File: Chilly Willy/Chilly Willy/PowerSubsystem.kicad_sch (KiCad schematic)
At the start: 8 parts, among them J1 Conn_01x03, U1 BK_HTC-15M

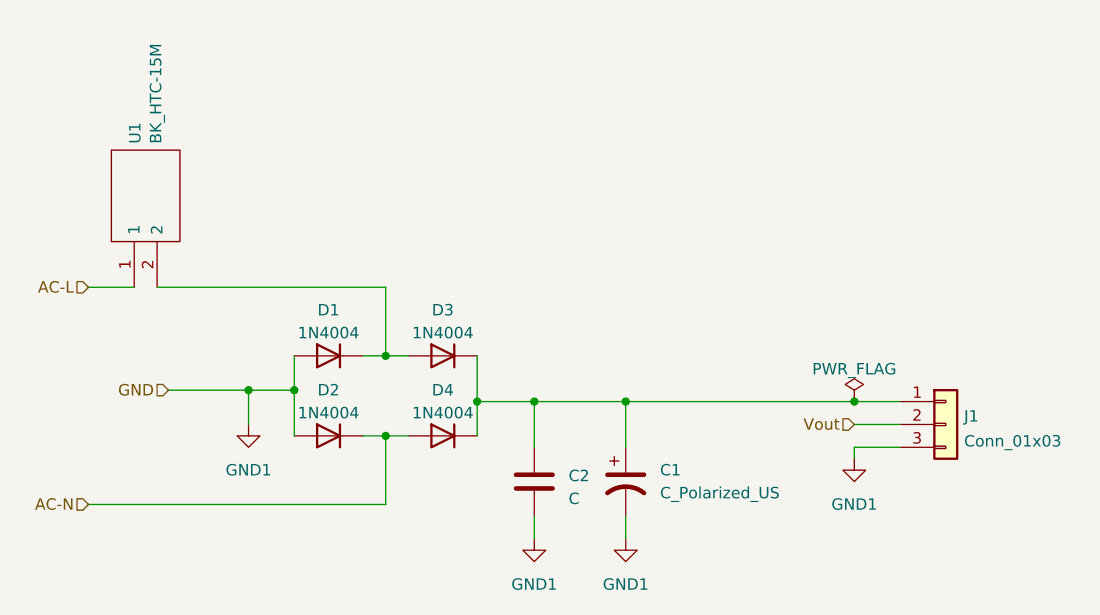
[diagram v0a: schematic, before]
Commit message: * adding in the Relays * GPIO via MCP23008
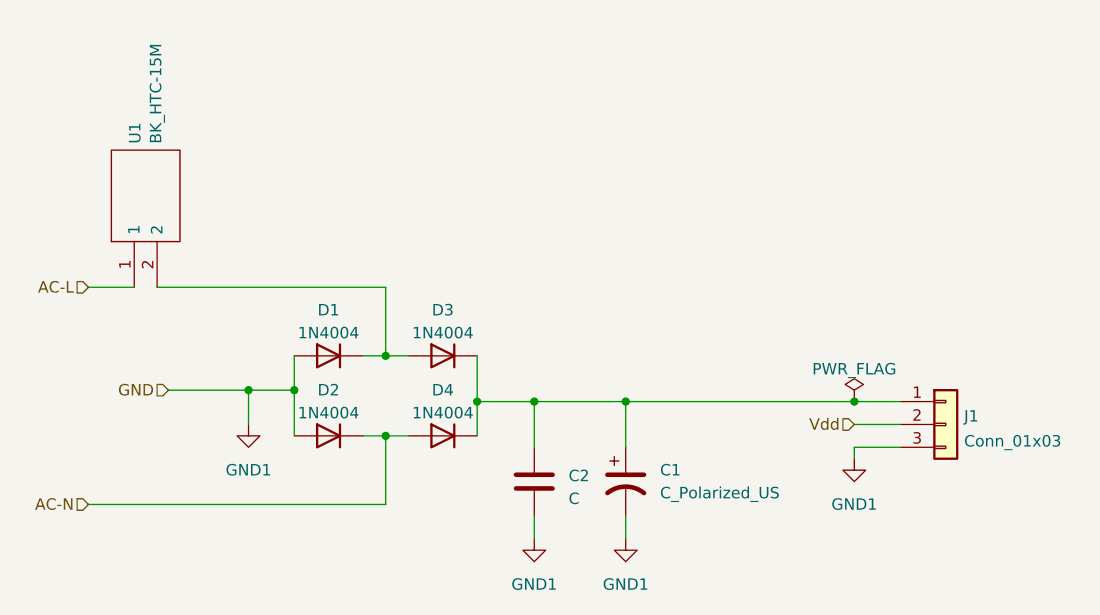
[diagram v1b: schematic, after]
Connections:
- net Vout renamed Vdd
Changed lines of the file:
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@@
     (stroke (width 0) (type default))
   )
-  (hierarchical_label "Vout" (shape input) (at 167.64 90.17 180) (fields_autoplaced)
+  (hierarchical_label "Vdd" (shape input) (at 167.64 90.17 180) (fields_autoplaced)
     (effects (font (size 1.27 1.27)) (justify right))
   )
